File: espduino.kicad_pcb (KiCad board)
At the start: 2 copper layers, 100 x 100 mm, 28 parts, among them IC101 ATMEGA168-A, P101 CONN_01X12, P102 CONN_01X12, P103 FTDI, P104 CONN_01X02, P401 CONN_01X02, P402 CONN_01X02, SW101 SPST, U201 74HCT125, U202 7400, U301 LSF0204x, U302 ESP8266, U401 LD1117S12TR, U402 LD1117S33TR, X101 16Mhz

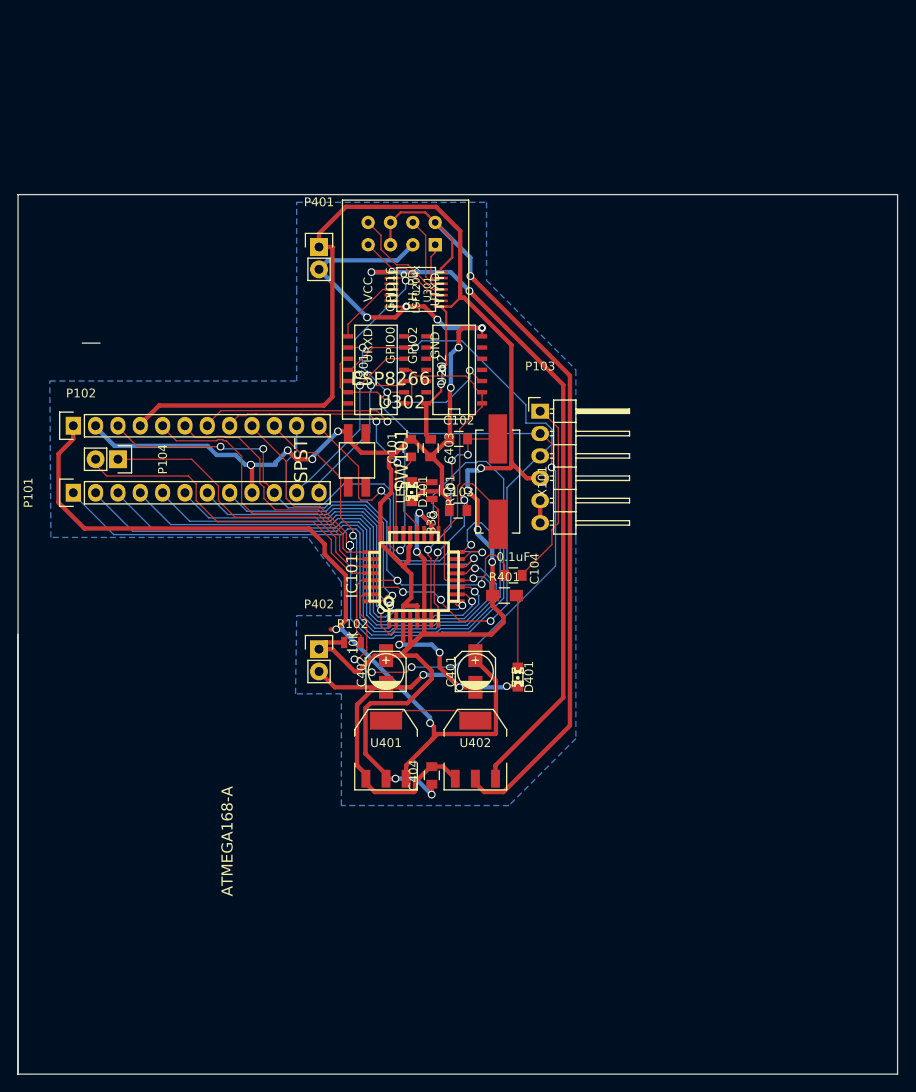
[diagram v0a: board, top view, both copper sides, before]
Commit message: Redesign the board and add USB
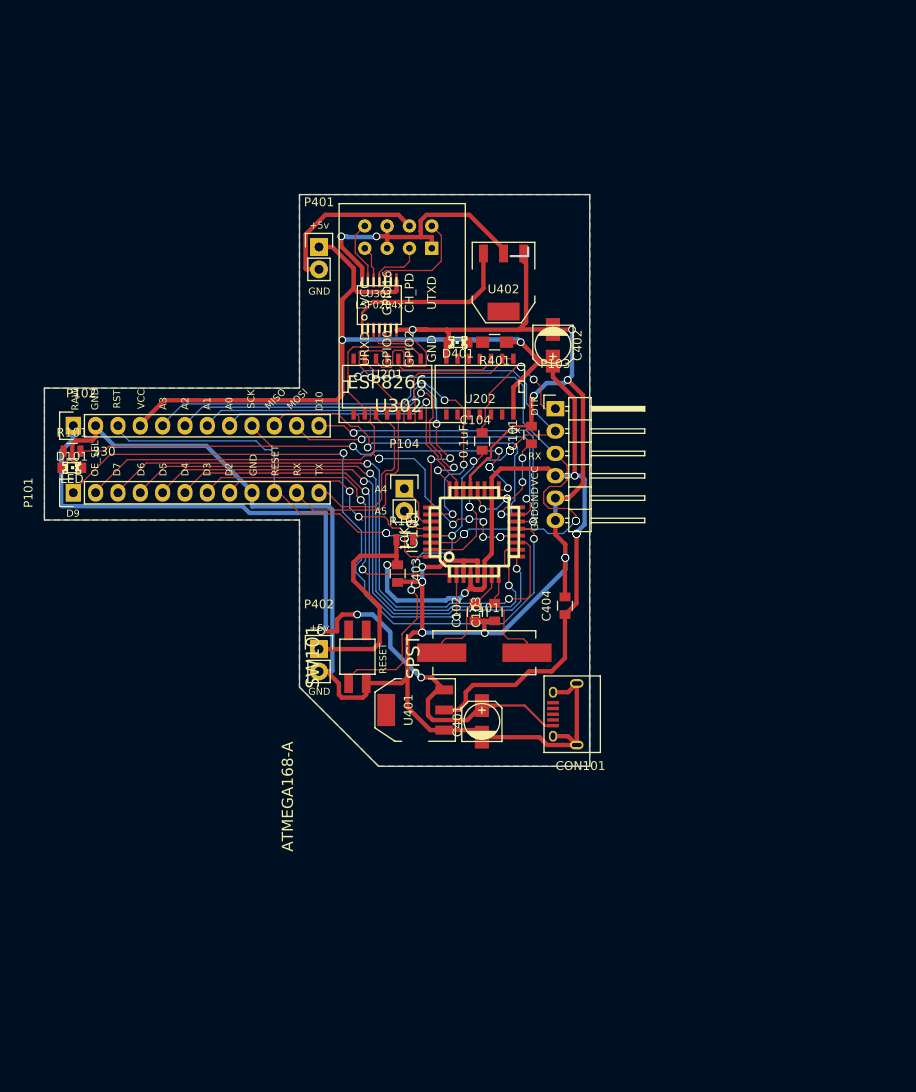
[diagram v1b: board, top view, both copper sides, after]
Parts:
- added CON101: USB-MICRO-B, Connect:USB_Micro-B, F.Cu at (135.8, 115.4)
- moved U402 53.2 mm to (130.2, 65.0), turned to 180 degrees
- moved C402 41.7 mm to (135.8, 72.1), turned to 270 degrees
- moved R101 41.1 mm to (81.1, 84.2), turned to 0 degrees
- moved D101 38.7 mm to (81.1, 86.1), turned to 0 degrees
- moved D401 38.7 mm to (125.0, 71.8), turned to 180 degrees
- moved P104 32.7 mm to (118.9, 88.4), turned to 0 degrees
- moved R401 28.8 mm to (129.2, 71.8), turned to 180 degrees
- moved U302 27.1 mm to (111.2, 78.2), turned to 0 degrees
- moved C404 24.5 mm to (137.2, 101.7)
- moved SW101 22.3 mm to (113.6, 107.5), turned to 90 degrees
- moved C102 19.8 mm to (126.9, 102.5), turned to 90 degrees
- moved X101 19.5 mm to (128.0, 107.1), turned to 0 degrees
- moved C104 15.6 mm to (127.8, 83.1), turned to 270 degrees
- moved C403 14.8 mm to (118.2, 98.1)
- moved C101 13.8 mm to (133.4, 82.3)
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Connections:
- U301 pad 2: /UART Selector/RX_2 -> (no net)
- U301 pad 3: (no net) -> /ESP Interface/RX
- U301 pad 4: /ESP Interface/RX -> (no net)
- U301 pad 5: (no net) -> /UART Selector/RX_2
- U302 pad 1: Net-(U301-Pad13) -> Net-(U301-Pad10)
- U302 pad 4: Net-(U301-Pad10) -> Net-(U301-Pad13)
- U302 pad 6: Net-(U301-Pad12) -> Net-(U301-Pad11)
- U302 pad 8: Net-(U301-Pad11) -> Net-(U301-Pad12)
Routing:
- net +3V3: track 93.9 -> 33.9 mm, vias 1 -> 2
- net +5V: track 77.0 -> 20.8 mm, vias 2 -> 0
- net GND: track 212.1 -> 267.9 mm, vias 16 -> 12
- net /A5: track 39.1 -> 4.24 mm
- net /A4: track 35.8 -> 5.62 mm
- net /SCK: track 85.1 -> 58.2 mm, vias 13 -> 5
- net /A3: track 34.3 -> 54.4 mm, vias 0 -> 3
- net /MISO: track 61.0 -> 42.6 mm
- net /UART Selector/TX: track 85.2 -> 68.8 mm, vias 6 -> 9
- net /A2: track 30.7 -> 46.7 mm, vias 0 -> 3
- net VCC: track 224.0 -> 208.0 mm, vias 10 -> 9
- net Net-(C103-Pad2): track 26.7 -> 11.7 mm, vias 2 -> 0
- net /RESET: track 73.8 -> 88.6 mm, vias 4 -> 5
- net Net-(C102-Pad2): track 26.6 -> 12.5 mm, vias 4 -> 0
- net /D5: track 47.9 -> 61.7 mm, vias 1 -> 2
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- added copper zone on F.Cu, net GND
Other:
- board size 100 x 100 mm -> 62 x 65 mm
- board text added: "+5v"
- board text added: "A0"
- board text added: "A1"
- board text added: "A2"
- board text added: "A3"
- board text added: "A4"
- board text added: "A5"
- board text added: "D10"
- board text added: "D2"
- board text added: "D3"
- board text added: "D4"
- board text added: "D5"
- board text added: "D6"
- board text added: "D7"
- board text added: "D9"
- board text added: "DTR"
- board text added: "GND"
- board text added: "MISO"
- board text added: "MOSI"
- board text added: "OE_SEL"
- board text added: "RAW"
- board text added: "RESET"
- board text added: "RST"
- board text added: "RX"
- board text added: "SCK"
- board text added: "TX"
- board text added: "Tx"
- board text added: "VCC"

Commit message: More fixes
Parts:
- added CON102: AVR-ISP-6, Pin_Headers:Pin_Header_Angled_2x03, F.Cu at (147.9, 86.5)
- added CON501: AVR-ISP-6, Pin_Headers:Pin_Header_Angled_2x03, F.Cu at (160.7, 105.9)
- added IC501: ATTINY25-SS, SMD_Packages:SOIC-8-N, F.Cu at (154.2, 98.7)
- added P105: CONN_01X03, Pin_Headers:Pin_Header_Straight_1x03, F.Cu at (161.7, 40.8)
- added P501: CONN_01X02, Pin_Headers:Pin_Header_Straight_1x02, F.Cu at (161.0, 95.4)
- added R501: R, Resistors_SMD:R_0805, F.Cu at (161.0, 100.6)
- added SP501: SPEAKER, Buzzers_Beepers:Buzzer_12x9.5RM7.6, B.Cu at (158.2, 98.4)
- CON101: footprint Connect:USB_Micro-B -> LittlebushLogicFootPrints:USB_Micro-B
- IC101: value ATMEGA168-A -> ATMEGA328-P
- P103: footprint Pin_Headers:Pin_Header_Angled_1x06 -> Pin_Headers:Pin_Header_Straight_1x06
- U302: footprint LittlebushLogicFootPrints:ESP8266 -> LittlebushLogicFootPrints:ESP8266_2
- moved X101 49.7 mm to (151.7, 63.3), turned to 180 degrees
- moved C404 46.0 mm to (134.6, 55.8), turned to 270 degrees
- moved C102 45.7 mm to (155.8, 67.0), turned to 180 degrees
- moved CON101 44.2 mm to (161.7, 79.6), turned to 90 degrees
- moved C103 42.1 mm to (141.6, 62.2), turned to 0 degrees
- moved C401 39.9 mm to (153.8, 84.7), turned to 180 degrees
- moved C104 38.6 mm to (158.7, 59.9)
- moved SW101 37.7 mm to (134.4, 76.1), turned to 270 degrees
- moved P104 36.3 mm to (154.3, 80.1), turned to 90 degrees
- moved C403 32.5 mm to (145.8, 81.0), turned to 0 degrees
- moved P103 32.2 mm to (161.7, 59.9)
- moved U401 32.1 mm to (135.5, 85.4), turned to 180 degrees
- moved C402 31.7 mm to (160.1, 51.8)
- moved D401 31.7 mm to (149.4, 51.4)
- moved U301 31.7 mm to (140.4, 47.2)
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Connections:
- CON101 pad 1: /Voltage Regulation/RAW -> VCC
- IC101 pad 1: /D3 -> /RESET
- IC101 pad 10: /D6 -> Net-(C103-Pad2)
- IC101 pad 11: /D7 -> /D5
- IC101 pad 12: /UART Selector/OE_Sel -> /D6
- IC101 pad 13: /D9 -> /D7
- IC101 pad 14: /D10 -> /UART Selector/OE_Sel
- IC101 pad 15: /MOSI -> /D9
- IC101 pad 16: /MISO -> /D10
- IC101 pad 17: /SCK -> /MOSI
- IC101 pad 18: VCC -> /MISO
- IC101 pad 19: (no net) -> /SCK
- IC101 pad 2: /D4 -> /UART Selector/RX
- IC101 pad 20: Net-(C101-Pad1) -> VCC
- IC101 pad 21: GND -> Net-(C101-Pad1)
- IC101 pad 22: (no net) -> GND
- IC101 pad 29: /RESET -> (no net)
- IC101 pad 3: GND -> /UART Selector/TX
- IC101 pad 30: /UART Selector/RX -> (no net)
- IC101 pad 31: /UART Selector/TX -> (no net)
- IC101 pad 32: /D2 -> (no net)
- IC101 pad 4: VCC -> /D2
- IC101 pad 5: GND -> /D3
- IC101 pad 6: VCC -> /D4
- IC101 pad 7: Net-(C102-Pad2) -> VCC
- IC101 pad 8: Net-(C103-Pad2) -> GND
- IC101 pad 9: /D5 -> Net-(C102-Pad2)
- U201 pad 1: /UART Selector/OE_Sel -> Net-(U201-Pad1)
- U201 pad 4: /UART Selector/OE_Sel -> Net-(U201-Pad1)
- U202 pad 10: (no net) -> /UART Selector/~PROG_EN
- U202 pad 3: Net-(U201-Pad10) -> Net-(U202-Pad3)
- U202 pad 4: (no net) -> /UART Selector/OE_Sel
- U202 pad 5: (no net) -> /UART Selector/~PROG_EN
- U202 pad 6: (no net) -> Net-(U201-Pad1)
- U202 pad 8: (no net) -> Net-(U201-Pad10)
- U202 pad 9: (no net) -> Net-(U202-Pad3)
- U301 pad 1: +5V -> VCC
- U402 pad 3: +5V -> VCC
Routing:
- net GND: track 267.9 -> 321.5 mm, vias 12 -> 20
- net /D9: track 81.5 -> 47.3 mm, vias 2 -> 3
- net Net-(IC501-Pad3): track 0.00 -> 28.0 mm, vias 0 -> 3
- net /UART Selector/~PROG_EN: track 0.00 -> 25.9 mm, vias 0 -> 1
- net /UART Selector/RX: track 71.5 -> 46.0 mm, vias 8 -> 3
- net /D7: track 71.0 -> 47.2 mm
- net /D6: track 66.3 -> 42.7 mm
- net /D5: track 61.7 -> 40.7 mm
- net Net-(CON501-Pad4): track 0.00 -> 21.0 mm
- net /UART Selector/TX: track 68.8 -> 47.9 mm, vias 9 -> 3
- net +5V: track 20.8 -> 0.00 mm
- net +3V3: track 33.9 -> 54.5 mm
- net Net-(U201-Pad1): track 0.00 -> 20.6 mm
- net /D10: track 36.7 -> 19.7 mm, vias 2 -> 0
- net Net-(CON501-Pad1): track 0.00 -> 16.9 mm
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- removed copper zone on B.Cu, net GND
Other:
- board size 62 x 65 mm -> 68.1 x 75.4 mm
- board text added: "PROG_EN"

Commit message: Version 0.2
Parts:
- removed CON501: AVR-ISP-6, Pin_Headers:Pin_Header_Angled_2x03
- removed IC501: ATTINY25-SS, SMD_Packages:SOIC-8-N
- removed P501: CONN_01X02, Pin_Headers:Pin_Header_Straight_1x02
- removed R501: R, Resistors_SMD:R_0805
- removed SP501: SPEAKER, Buzzers_Beepers:Buzzer_12x9.5RM7.6
- added BT1: Battery, Pin_Headers:Pin_Header_Straight_1x01, F.Cu at (161.3, 93.7)
- added C601: 1uF, Capacitors_SMD:C_0805, F.Cu at (137.2, 110.5)
- added C602: 1uF, Capacitors_SMD:C_0805, F.Cu at (142.5, 104.6)
- added CON1: AVR-ISP-6, Pin_Headers:Pin_Header_Straight_2x03, F.Cu at (151.9, 97.5)
- added CON601: BARREL_JACK, Connect:BARREL_JACK, F.Cu at (133.4, 96.3)
- added D601: LED, LEDs:LED-0805, F.Cu at (131.6, 102.1)
- added D602: LED, LEDs:LED-0805, F.Cu at (131.6, 105.7)
- added IC1: ATTINY85-S, ab2_so:AB2_SO08, F.Cu at (157.1, 109.8)
- added IC2: ATTINY85-P, Housings_DIP:DIP-8_W7.62mm, F.Cu at (152.9, 113.5)
- added P1: CONN_01X02, Pin_Headers:Pin_Header_Straight_1x02, F.Cu at (160.6, 97.5)
- added P601: BATT+, Pin_Headers:Pin_Header_Straight_1x01, F.Cu at (142.5, 101.6)
- added R1: R, Resistors_SMD:R_0805, F.Cu at (151.8, 93.5)
- added R601: 10K, Resistors_SMD:R_0805, F.Cu at (137.0, 103.8)
- added R602: 1K, Resistors_SMD:R_0805, F.Cu at (131.8, 103.9)
- added R603: 1K, Resistors_SMD:R_0805, F.Cu at (131.8, 107.4)
- added R604: R, Resistors_SMD:R_0805, F.Cu at (141.7, 108.8)
- added SP1: SPEAKER, footprints:buzzer, B.Cu at (157.1, 97.4)
- added U601: LM3658, footprints:WSON10, F.Cu at (142.1, 105.2)
- CON101: footprint LittlebushLogicFootPrints:USB_Micro-B -> footprints:USB_Micro-B
- CON102: footprint Pin_Headers:Pin_Header_Angled_2x03 -> Pin_Headers:Pin_Header_Straight_2x03
- IC101: value ATMEGA328-P -> ATMEGA328P-A; footprint LittlebushLogicFootPrints:TQFP32_08 -> footprints:TQFP32_08
- P101: value CONN_01X12 -> CONN_01X03; footprint Pin_Headers:Pin_Header_Straight_1x12 -> Pin_Headers:Pin_Header_Straight_1x03
- P103: value FTDI -> CONN_01X12; footprint Pin_Headers:Pin_Header_Straight_1x06 -> Pin_Headers:Pin_Header_Straight_1x12
- P104: value CONN_01X02 -> FTDI; footprint Pin_Headers:Pin_Header_Straight_1x02 -> Pin_Headers:Pin_Header_Straight_1x06
- P105: value CONN_01X03 -> CONN_01X02; footprint Pin_Headers:Pin_Header_Straight_1x03 -> Pin_Headers:Pin_Header_Straight_1x02
- SW101: footprint LittlebushLogicFootPrints:4x4_Tactile_SMD_switch -> footprints:4x4_Tactile_SMD_switch
- U301: footprint AB2_TSSOP:AB2_TSSOP14 -> ab2_tssop:AB2_TSSOP14
- U302: footprint LittlebushLogicFootPrints:ESP8266_2 -> footprints:ESP8266_2
- moved P101 66.3 mm to (160.3, 39.8), turned to 0 degrees
- moved P103 62.4 mm to (99.4, 60.9), turned to 90 degrees
- moved P105 47.9 mm to (157.0, 88.5), turned to 90 degrees
- moved P104 21.3 mm to (160.3, 59.7), turned to 0 degrees
- moved P102 7.73 mm to (99.4, 68.5)
- moved CON101 2.09 mm to (160.5, 81.3)
- moved SW101 1.95 mm to (132.8, 77.1)
- moved U401 1.47 mm to (134.7, 86.6), turned to 270 degrees
- moved CON102 1.28 mm to (146.6, 86.4)
- moved C101 1.27 mm to (148.8, 81.6)
- moved C102 1.27 mm to (154.5, 67.0)
- moved C103 1.27 mm to (140.3, 62.2)
- moved C404 1.27 mm to (133.3, 55.8)
- moved D401 1.27 mm to (148.1, 51.4)
- moved R101 1.27 mm to (98.6, 63.8)
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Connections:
- IC101 pad 1: /RESET -> /D3
- IC101 pad 10: Net-(C103-Pad2) -> /D6
- IC101 pad 11: /D5 -> /D7
- IC101 pad 12: /D6 -> /UART Selector/OE_Sel
- IC101 pad 13: /D7 -> /D9
- IC101 pad 14: /UART Selector/OE_Sel -> /D10
- IC101 pad 15: /D9 -> /MOSI
- IC101 pad 16: /D10 -> /MISO
- IC101 pad 17: /MOSI -> /SCK
- IC101 pad 18: /MISO -> VCC
- IC101 pad 19: /SCK -> (no net)
- IC101 pad 2: /UART Selector/RX -> /D4
- IC101 pad 20: VCC -> Net-(C101-Pad1)
- IC101 pad 21: Net-(C101-Pad1) -> (no net)
- IC101 pad 22: GND -> (no net)
- IC101 pad 29: (no net) -> /RESET
- IC101 pad 3: /UART Selector/TX -> GND
- IC101 pad 30: (no net) -> /UART Selector/RX
- IC101 pad 31: (no net) -> /UART Selector/TX
- IC101 pad 32: (no net) -> /D2
- IC101 pad 4: /D2 -> VCC
- IC101 pad 5: /D3 -> GND
- IC101 pad 6: /D4 -> (no net)
- IC101 pad 7: VCC -> Net-(C102-Pad2)
- IC101 pad 8: GND -> Net-(C103-Pad2)
- IC101 pad 9: Net-(C102-Pad2) -> /D5
- P101 pad 1: /D9 -> GND
- P101 pad 2: /UART Selector/OE_Sel -> /UART Selector/~PROG_EN
- P101 pad 3: /D7 -> VCC
- P102 pad 1: /Voltage Regulation/RAW -> /D9
- P102 pad 10: /MISO -> /RESET
- P102 pad 11: /MOSI -> /UART Selector/RX_1
- P102 pad 12: /D10 -> /UART Selector/TX_1
- P102 pad 2: GND -> /UART Selector/OE_Sel
- P102 pad 3: /RESET -> /D7
- P102 pad 4: VCC -> /D6
- P102 pad 5: /A3 -> /D5
- P102 pad 6: /A2 -> /D4
- P102 pad 7: /A1 -> /D3
- P102 pad 8: /A0 -> /D2
- P102 pad 9: /SCK -> GND
- P103 pad 1: /DTR -> /Voltage Regulation/RAW
- P103 pad 2: /UART Selector/TX -> GND
- P103 pad 3: /UART Selector/RX -> /RESET
- P103 pad 5: GND -> /A3
- P103 pad 6: GND -> /A2
- P104 pad 1: /A4 -> /DTR
- P104 pad 2: /A5 -> /UART Selector/TX
- P105 pad 1: GND -> /A4
- P105 pad 2: /UART Selector/~PROG_EN -> /A5
- U302 pad 2: GND -> +3V3
- U302 pad 4: Net-(U301-Pad13) -> +3V3
- U302 pad 5: +3V3 -> GND
- U302 pad 6: Net-(U301-Pad11) -> Net-(U301-Pad13)
- U302 pad 7: +3V3 -> Net-(U301-Pad11)
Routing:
- net GND: track 321.5 -> 431.1 mm, vias 20 -> 27
- net /UART Selector/TX_1: track 21.7 -> 88.6 mm, vias 1 -> 2
- net /UART Selector/RX_1: track 26.2 -> 91.1 mm, vias 1 -> 2
- net /Freezy/ADC: track 0.00 -> 51.4 mm
- net Net-(BT1-Pad1): track 0.00 -> 38.3 mm
- net /Freezy/MOSI: track 0.00 -> 29.4 mm, vias 0 -> 1
- net Net-(IC501-Pad3): track 28.0 -> 0.00 mm, vias 3 -> 0
- net +6V: track 0.00 -> 27.2 mm
- net Net-(R604-Pad2): track 0.00 -> 26.6 mm
- net /Freezy/~RST: track 0.00 -> 22.3 mm
- net /RESET: track 80.9 -> 102.4 mm, vias 6 -> 4
- net VCC: track 224.3 -> 245.4 mm, vias 7 -> 8
- net Net-(CON501-Pad4): track 21.0 -> 0.00 mm
- net /SCK: track 69.0 -> 89.6 mm, vias 2 -> 5
- net +3V3: track 54.5 -> 35.0 mm, vias 2 -> 0
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- added copper zone on B.Cu, net GND
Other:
- board size 68.1 x 75.4 mm -> 67.7 x 79.8 mm
- net class Charger added: clearance 0.127, trace_width 0.127, via_dia 0.889, via_drill 0.635
- net class Default: clearance 0.254 -> 0.127
- net class Power: clearance 0.254 -> 0.127
- rule trace_clearance: 0.254 -> 0.127
- board text added: "Espduino V0.2"
- board text added: "Littlebush Logic"

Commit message: Minor changes
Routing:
- net Net-(D602-Pad2): track 0.00 -> 1.92 mm
- net Net-(D601-Pad2): track 0.00 -> 1.92 mm
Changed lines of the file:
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@@
     (thickness 1.6)
     (drawings 104)
-    (tracks 1113)
+    (tracks 1117)
     (zones 0)
     (modules 49)
@@
   (segment (start 152.796599 103.564823) (end 152.796599 103.459599) (width 0.127) (layer F.Cu) (net 34))
   (segment (start 152.796599 103.459599) (end 151.933 102.596) (width 0.127) (layer F.Cu) (net 34))
+  (segment (start 130.52298 102.108) (end 130.52298 103.53298) (width 0.127) (layer F.Cu) (net 35))
+  (segment (start 130.52298 103.53298) (end 130.876 103.886) (width 0.127) (layer F.Cu) (net 35))
   (segment (start 134.3435 106.049724) (end 134.3435 103.10404) (width 0.127) (layer F.Cu) (net 36))
   (segment (start 134.3435 103.10404) (end 133.34746 102.108) (width 0.127) (layer F.Cu) (net 36))
@@
   (segment (start 135.76 107.18) (end 135.473776 107.18) (width 0.127) (layer F.Cu) (net 36))
   (segment (start 135.473776 107.18) (end 134.3435 106.049724) (width 0.127) (layer F.Cu) (net 36))
+  (segment (start 130.52298 105.664) (end 130.52298 107.08898) (width 0.127) (layer F.Cu) (net 37))
+  (segment (start 130.52298 107.08898) (end 130.876 107.442) (width 0.127) (layer F.Cu) (net 37))
   (segment (start 134.08949 106.154938) (end 133.598552 105.664) (width 0.127) (layer F.Cu) (net 38))
   (segment (start 133.598552 105.664) (end 132.62102 105.664) (width 0.127) (layer F.Cu) (net 38))
